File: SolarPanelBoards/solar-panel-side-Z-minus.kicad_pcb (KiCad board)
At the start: 2 copper layers, 97 x 97.4 mm, 43 parts, among them J1 Conn_01x06, J2 SMA Connector Male, Q12 BSS138DWQ-7, Q13 BSS138DWQ-7, Q7 MBT2222ADW1T1, Q8 MBT2222ADW1T1, U1 OPT3001DNPT, U2 HHM1589D1

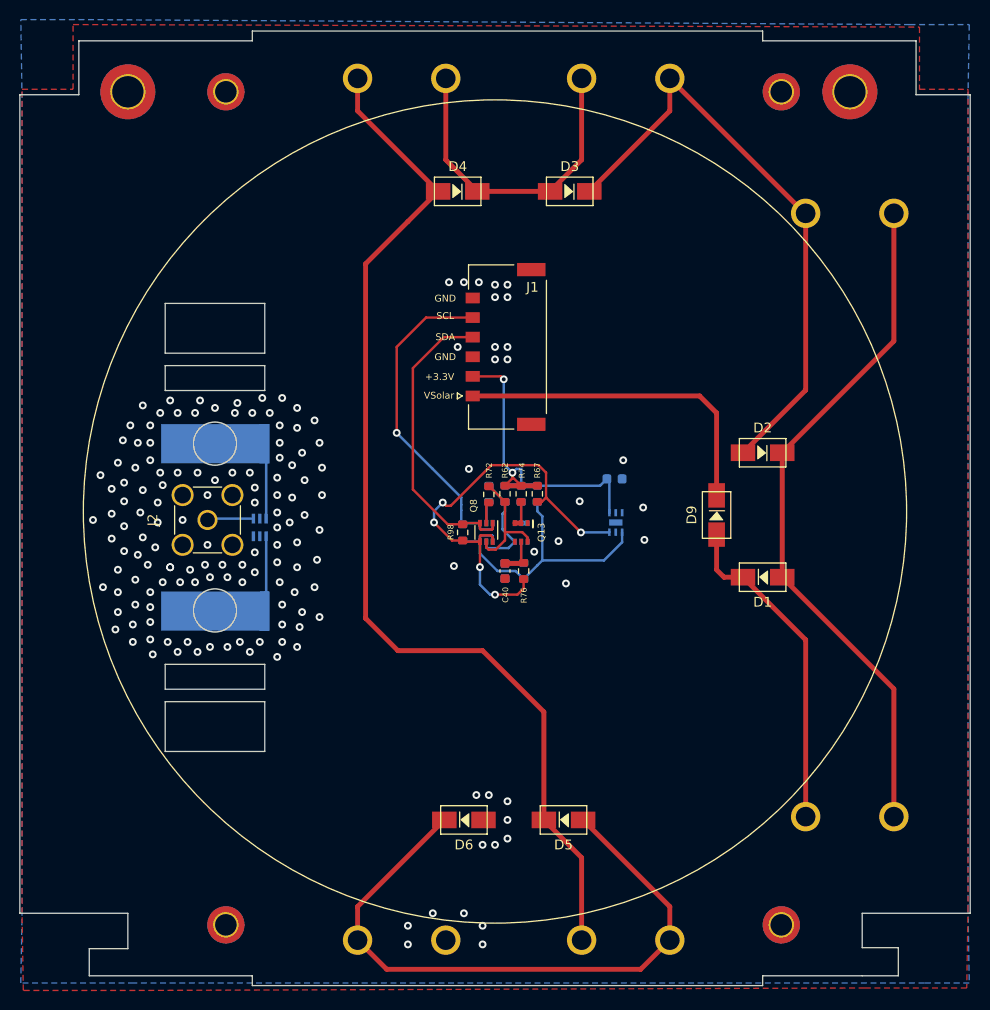
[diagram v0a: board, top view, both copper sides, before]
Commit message: Z- finished, new radio traces and edges
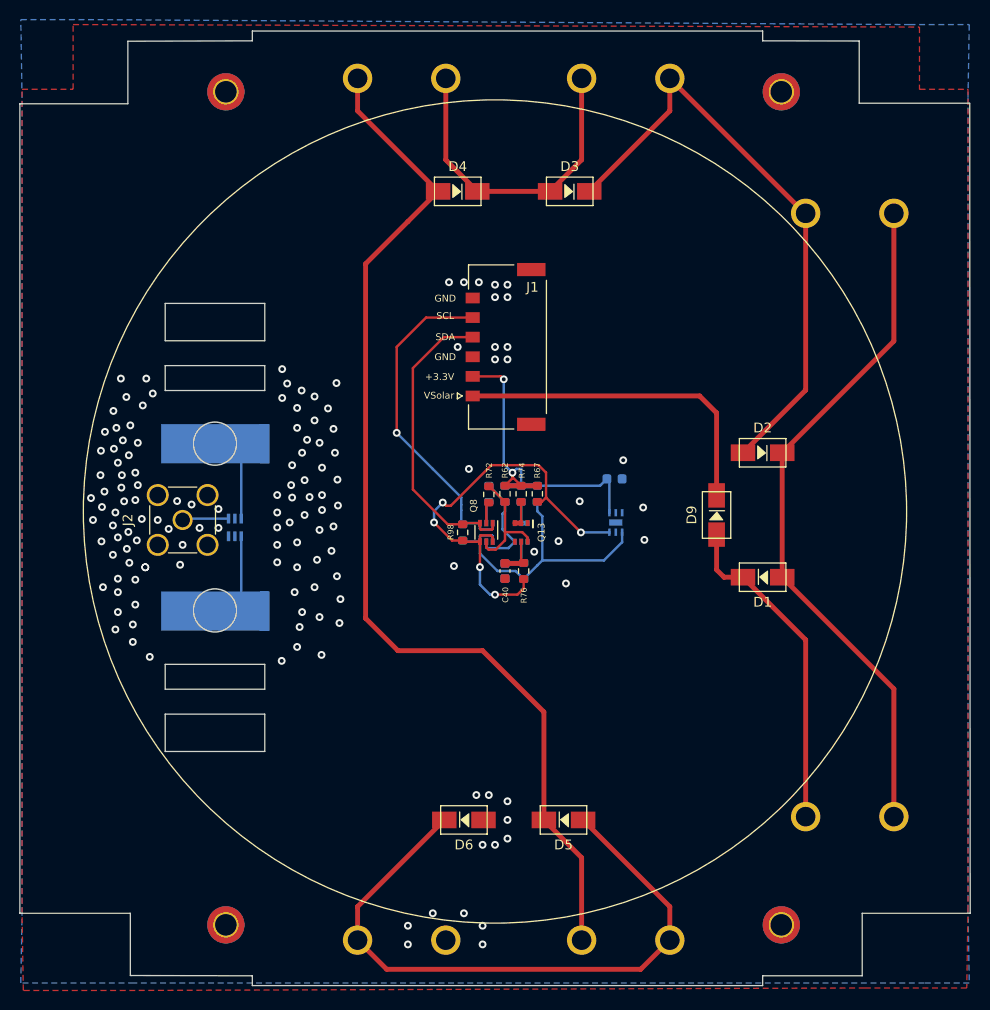
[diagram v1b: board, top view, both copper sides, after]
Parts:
- removed H1, H2: MountingHole_Pad, MountingHole:MountingHole_3.2mm_M3_DIN965_Pad_TopBottom
- moved J2 2.54 mm to (116.1, 95.8)
- moved U2 2.54 mm to (121.4, 96.5)
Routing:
- net GND: vias 157 -> 140
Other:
- outline, holes or cut-outs redrawn
- net class RF 200 added: clearance 1.8, trace_width 0.25, via_dia 0.8, via_drill 0.4
- net class RF 50 added: clearance 0.122, trace_width 0.4, via_dia 0.8, via_drill 0.4
